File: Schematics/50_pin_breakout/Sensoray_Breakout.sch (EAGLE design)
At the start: 26 parts, among them J1 22-27-2021-02, J10 22-27-2021-02, J2 22-27-2021-02, J21 22-27-2021-02, J22 22-27-2021-02, J23 22-27-2021-02, J24 22-27-2021-02, J25 22-27-2021-02, J26 22-27-2021-02, J27 22-27-2021-02, J28 22-27-2021-02, J29 22-27-2021-02, J3 22-27-2021-02, J30 22-27-2021-02, J31 22-27-2021-02, J32 22-27-2021-02, J33 22-27-2021-02, J34 22-27-2021-02, J35 22-27-2021-02, J4 22-27-2021-02, J5 22-27-2021-02, J6 22-27-2021-02, J7 22-27-2021-02, J8 22-27-2021-02, J9 22-27-2021-02, X1 87758-5016

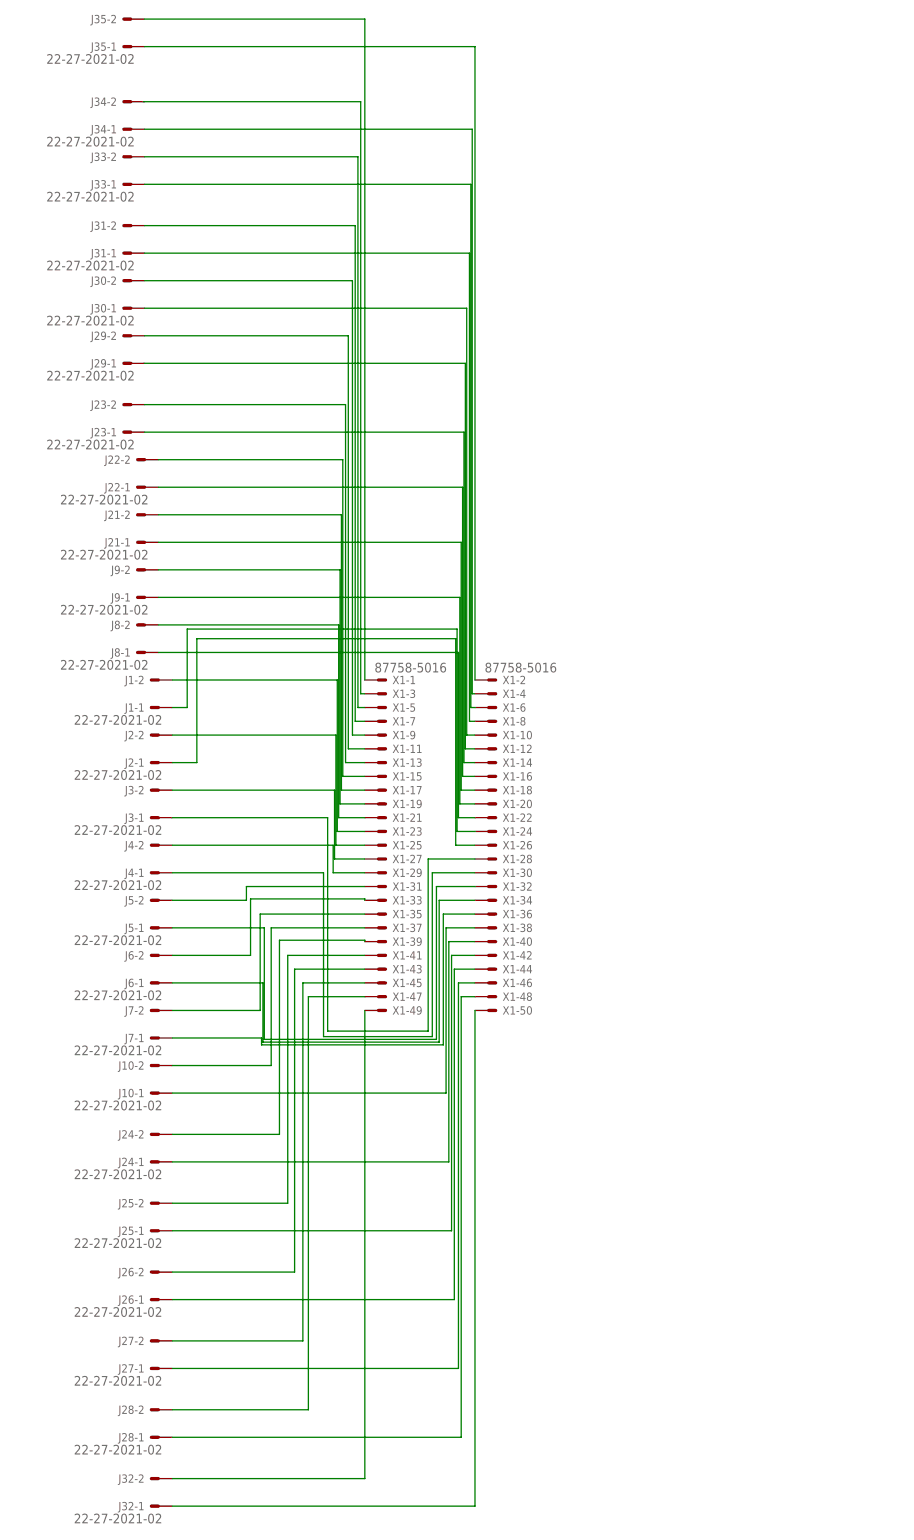
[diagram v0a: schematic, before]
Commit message: added Rev 2 for 26 and 50 pin breakout boards, along with their gerber files for 1-layer PCB use. also added WPR for week of 27th
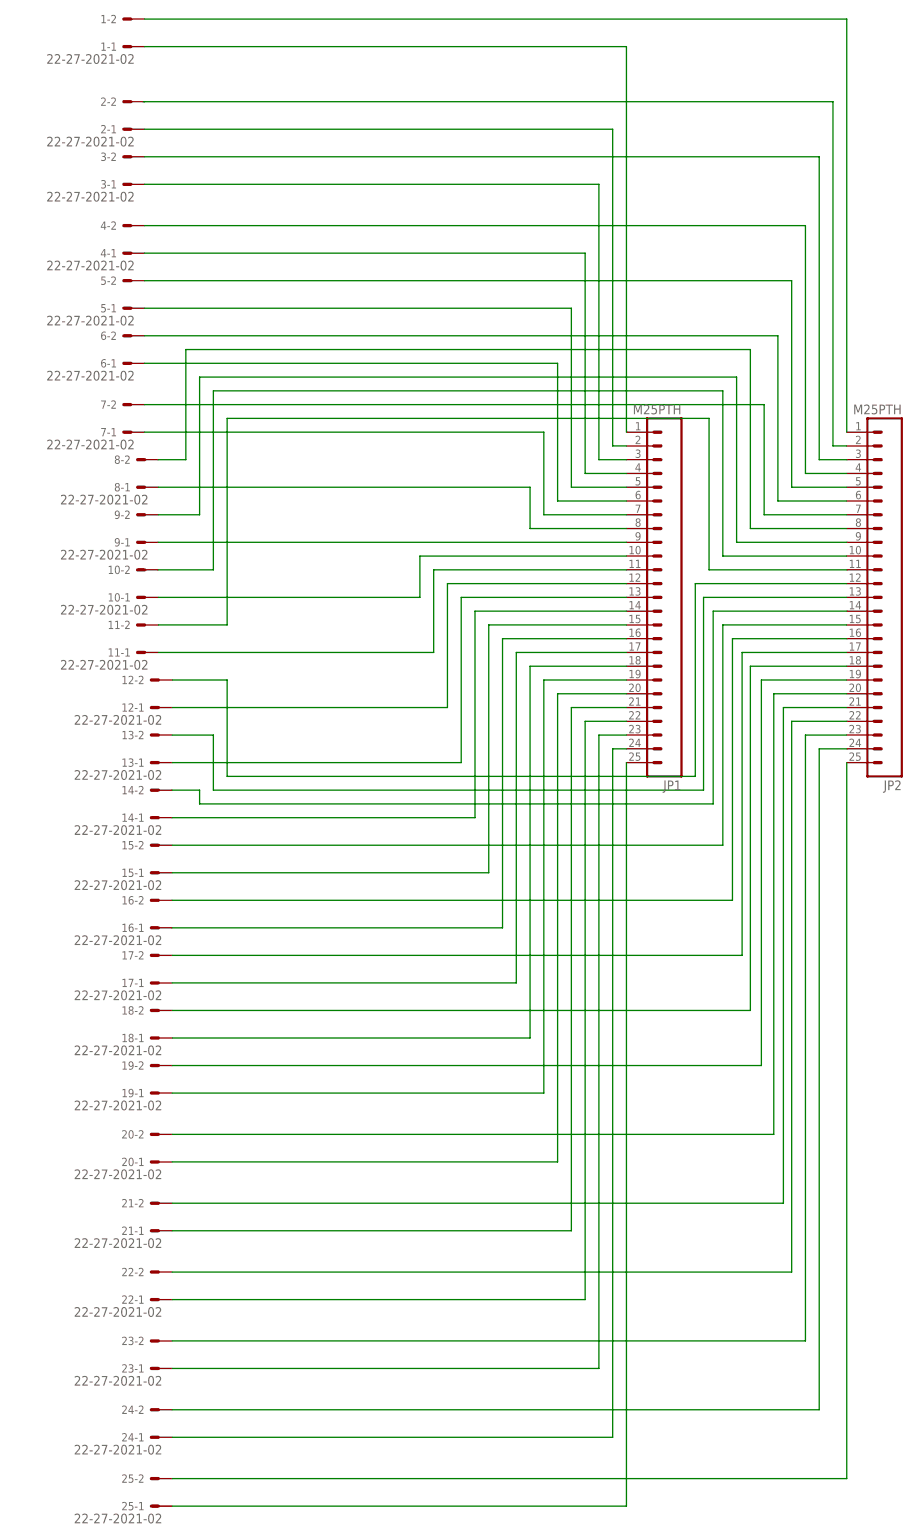
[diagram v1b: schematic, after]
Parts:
- removed X1: 87758-5016, con-molex:87758-5016
- added JP1, JP2: M25PTH, SparkFun-Connectors:M25PTH
- renumbered J1 to 12, J10 to 19, J2 to 13, J21 to 9, J22 to 8, J23 to 7, J24 to 20, J25 to 21, J26 to 22, J27 to 23, J28 to 24, J29 to 6, J3 to 14, J30 to 5, J31 to 4, J32 to 25, J33 to 3, J34 to 2, J35 to 1, J4 to 15, J5 to 16, J6 to 17, J7 to 18, J8 to 11, J9 to 10
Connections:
- net N$1: now also 1-1.S, JP1.1; no longer 1-2.S, X1-1.S
- net N$10: now also 9-1.S, JP1.9; no longer 8-2.S, X1-15.S
- net N$11: now also 25-1.S, JP1.25; no longer 9-2.S, X1-17.S
- net N$12: now also 24-1.S, JP1.24; no longer 10-2.S, X1-19.S
- net N$13: now also 23-1.S, JP1.23; no longer 11-2.S, X1-21.S
- net N$14: now also 22-1.S, JP1.22; no longer 12-2.S, X1-23.S
- net N$15: now also 21-1.S, JP1.21; no longer 13-2.S, X1-25.S
- net N$16: now also 20-1.S, JP1.20; no longer 3-1.S, X1-6.S
- net N$17: now also 19-1.S, JP1.19; no longer 4-1.S, X1-8.S
- net N$18: now also 18-1.S, JP1.18; no longer 5-1.S, X1-10.S
- net N$19: now also 17-1.S, JP1.17; no longer 6-1.S, X1-12.S
- net N$2: now also 2-1.S, JP1.2; no longer 1-1.S, X1-2.S
- net N$20: now also 16-1.S, JP1.16; no longer 7-1.S, X1-14.S
- net N$21: now also 15-1.S, JP1.15; no longer 8-1.S, X1-16.S
- net N$22: now also 14-1.S, JP1.14; no longer 9-1.S, X1-18.S
- net N$23: now also 13-1.S, JP1.13; no longer 10-1.S, X1-20.S
- net N$24: now also 12-1.S, JP1.12; no longer 11-1.S, X1-22.S
- net N$25: now also 11-1.S, JP1.11; no longer 12-1.S, X1-24.S
- net N$26: now also 10-1.S, JP1.10; no longer 13-1.S, X1-26.S
- net N$27: now also 1-2.S, JP2.1; no longer 14-2.S, X1-27.S
- net N$28: now also 3-2.S, JP2.3; no longer 15-2.S, X1-29.S
- net N$29: now also 4-2.S, JP2.4; no longer 16-2.S, X1-31.S
- net N$3: now also 2-2.S, JP2.2; no longer X1-3.S
- net N$30: now also 5-2.S, JP2.5; no longer 17-2.S, X1-33.S
- net N$31: now also 6-2.S, JP2.6; no longer 18-2.S, X1-35.S
- net N$32: now also 7-2.S, JP2.7; no longer 19-2.S, X1-37.S
- net N$33: now also 8-2.S, JP2.8; no longer 20-2.S, X1-39.S
- net N$34: now also 9-2.S, JP2.9; no longer 21-2.S, X1-41.S
- net N$35: now also 10-2.S, JP2.10; no longer 22-2.S, X1-43.S
- net N$36: now also 11-2.S, JP2.11; no longer 23-2.S, X1-45.S
- net N$37: now also 12-2.S, JP2.12; no longer 24-2.S, X1-47.S
- net N$38: now also 13-2.S, JP2.13; no longer 25-2.S, X1-49.S
- net N$39: now also 14-2.S, JP2.14; no longer 14-1.S, X1-28.S
- net N$4: now also 3-1.S, JP1.3; no longer 2-1.S, X1-4.S
- net N$40: now also 15-2.S, JP2.15; no longer 15-1.S, X1-30.S
- net N$41: now also 16-2.S, JP2.16; no longer 16-1.S, X1-32.S
- net N$42: now also 17-2.S, JP2.17; no longer 17-1.S, X1-34.S
- net N$43: now also 18-2.S, JP2.18; no longer 18-1.S, X1-36.S
- net N$44: now also 19-2.S, JP2.19; no longer 19-1.S, X1-38.S
- net N$45: now also 20-2.S, JP2.20; no longer 20-1.S, X1-40.S
- net N$46: now also 21-2.S, JP2.21; no longer 21-1.S, X1-42.S
- net N$47: now also 22-2.S, JP2.22; no longer 22-1.S, X1-44.S
- net N$48: now also 23-2.S, JP2.23; no longer 23-1.S, X1-46.S
- net N$49: now also 24-2.S, JP2.24; no longer 24-1.S, X1-48.S
- net N$5: now also 4-1.S, JP1.4; no longer 3-2.S, X1-5.S
- net N$50: now also 25-2.S, JP2.25; no longer 25-1.S, X1-50.S
- net N$6: now also 5-1.S, JP1.5; no longer 4-2.S, X1-7.S
- net N$7: now also 6-1.S, JP1.6; no longer 5-2.S, X1-9.S
- net N$8: now also 7-1.S, JP1.7; no longer 6-2.S, X1-11.S
- net N$9: now also 8-1.S, JP1.8; no longer 7-2.S, X1-13.S
